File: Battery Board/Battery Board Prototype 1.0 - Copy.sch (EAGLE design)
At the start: 10 parts

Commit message: Added separation notches
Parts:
- added J1, J2: MPTC-02-16-02-6.30-XX-X-V, MPTC-02-16-02-6.30-XX-X-V:MPTC-02-16-02-6.30-XX-X-V
- added J3: TFM-107-01-XXX-D-DS, TFM-107-01-XXX-D-DS:TFM-107-01-XXX-D-DS
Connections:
- new net AUX0: U$1.PB1
- new net AUX1: U$1.PB2
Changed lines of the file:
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@@
 <part name="R6" library="resistor" library_urn="urn:adsk.eagle:library:348" deviceset="R-US_" device="R0805" package3d_urn="urn:adsk.eagle:package:23553/2"/>
 <part name="R7" library="resistor" library_urn="urn:adsk.eagle:library:348" deviceset="R-US_" device="R0805" package3d_urn="urn:adsk.eagle:package:23553/2"/>
+<part name="J1" library="MPTC-02-16-02-6.30-XX-X-V" deviceset="MPTC-02-16-02-6.30-XX-X-V" device=""/>
+<part name="J2" library="MPTC-02-16-02-6.30-XX-X-V" deviceset="MPTC-02-16-02-6.30-XX-X-V" device=""/>
+<part name="J3" library="TFM-107-01-XXX-D-DS" deviceset="TFM-107-01-XXX-D-DS" device=""/>
 </parts>
 <sheets>
@@
 <attribute name="VALUE" x="-52.07" y="-6.858" size="1.778" layer="96" rot="R180"/>
 </instance>
+<instance part="J1" gate="G$1" x="48.26" y="63.5" smashed="yes">
+<attribute name="NAME" x="38.1" y="80.01" size="1.778" layer="95"/>
+<attribute name="VALUE" x="38.1" y="43.18" size="1.778" layer="96"/>
+</instance>
+<instance part="J2" gate="G$1" x="127" y="50.8" smashed="yes">
+<attribute name="NAME" x="116.84" y="67.31" size="1.778" layer="95"/>
+<attribute name="VALUE" x="116.84" y="30.48" size="1.778" layer="96"/>
+</instance>
+<instance part="J3" gate="G$1" x="-50.8" y="78.74" smashed="yes">
+<attribute name="NAME" x="-45.72" y="82.042" size="1.27" layer="95"/>
+<attribute name="VALUE" x="-45.72" y="48.26" size="1.27" layer="96"/>
+</instance>
 </instances>
 <busses>
@@
 </segment>
 <segment>
-<wire x1="22.86" y1="35.56" x2="22.86" y2="27.94" width="0.1524" layer="91"/>
-<label x="22.86" y="27.94" size="1.27" layer="95" rot="R270" xref="yes"/>
+<wire x1="27.94" y1="35.56" x2="27.94" y2="27.94" width="0.1524" layer="91"/>
+<label x="27.94" y="27.94" size="1.27" layer="95" rot="R270" xref="yes"/>
 </segment>
 </net>
@@
 </segment>
 <segment>
-<wire x1="25.4" y1="27.94" x2="25.4" y2="35.56" width="0.1524" layer="91"/>
-<label x="25.4" y="27.94" size="1.27" layer="95" rot="R270" xref="yes"/>
+<wire x1="30.48" y1="27.94" x2="30.48" y2="35.56" width="0.1524" layer="91"/>
+<label x="30.48" y="27.94" size="1.27" layer="95" rot="R270" xref="yes"/>
 </segment>
 </net>
@@
 </segment>
 <segment>
-<wire x1="20.32" y1="35.56" x2="20.32" y2="27.94" width="0.1524" layer="91"/>
-<label x="20.32" y="27.94" size="1.27" layer="95" rot="R270" xref="yes"/>
+<wire x1="22.86" y1="35.56" x2="22.86" y2="27.94" width="0.1524" layer="91"/>
+<label x="22.86" y="27.94" size="1.27" layer="95" rot="R270" xref="yes"/>
 </segment>
 </net>
@@
 </segment>
 <segment>
-<wire x1="15.24" y1="27.94" x2="15.24" y2="35.56" width="0.1524" layer="91"/>
-<label x="15.24" y="27.94" size="1.27" layer="95" rot="R270" xref="yes"/>
+<wire x1="12.7" y1="27.94" x2="12.7" y2="35.56" width="0.1524" layer="91"/>
+<label x="12.7" y="27.94" size="1.27" layer="95" rot="R270" xref="yes"/>
 </segment>
 </net>
@@
 <label x="55.88" y="12.7" size="1.27" layer="95" rot="R270" xref="yes"/>
 </segment>
+<segment>
+<wire x1="15.24" y1="35.56" x2="15.24" y2="27.94" width="0.1524" layer="91"/>
+<label x="15.24" y="27.94" size="1.27" layer="95" rot="R270" xref="yes"/>
+</segment>
 </net>
 <net name="SDA" class="0">
@@
 </segment>
 </net>
+<net name="AUX1" class="0">
+<segment>
+<pinref part="U$1" gate="U$1" pin="PB2"/>
+<wire x1="20.32" y1="2.54" x2="22.86" y2="2.54" width="0.1524" layer="91"/>
+<label x="22.86" y="2.54" size="1.27" layer="95" xref="yes"/>
+</segment>
+<segment>
+<wire x1="20.32" y1="35.56" x2="20.32" y2="27.94" width="0.1524" layer="91"/>
+<label x="20.32" y="27.94" size="1.27" layer="95" rot="R270" xref="yes"/>
+</segment>
+</net>
+<net name="AUX0" class="0">
+<segment>
+<pinref part="U$1" gate="U$1" pin="PB1"/>
+<wire x1="20.32" y1="-2.54" x2="22.86" y2="-2.54" width="0.1524" layer="91"/>
+<label x="22.86" y="-2.54" size="1.27" layer="95" xref="yes"/>
+</segment>
+<segment>
+<wire x1="25.4" y1="35.56" x2="25.4" y2="27.94" width="0.1524" layer="91"/>
+<label x="25.4" y="27.94" size="1.27" layer="95" rot="R270" xref="yes"/>
+</segment>
+</net>

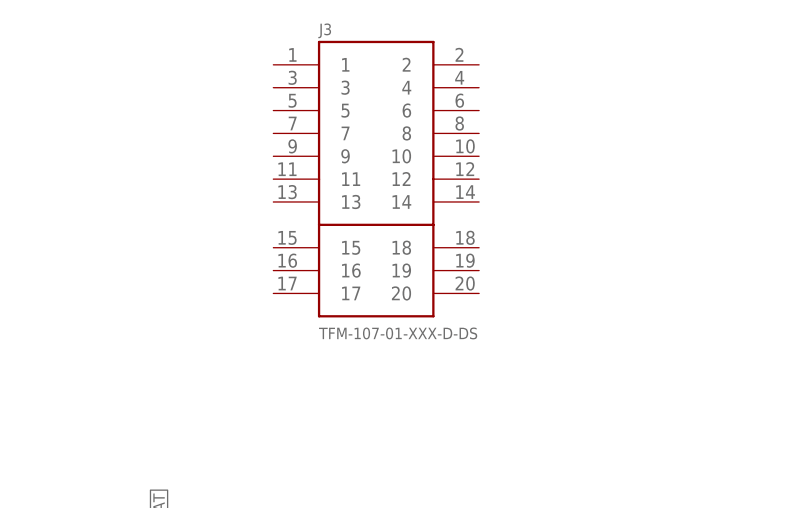
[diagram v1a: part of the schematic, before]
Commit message: Improved Battery board interface nets
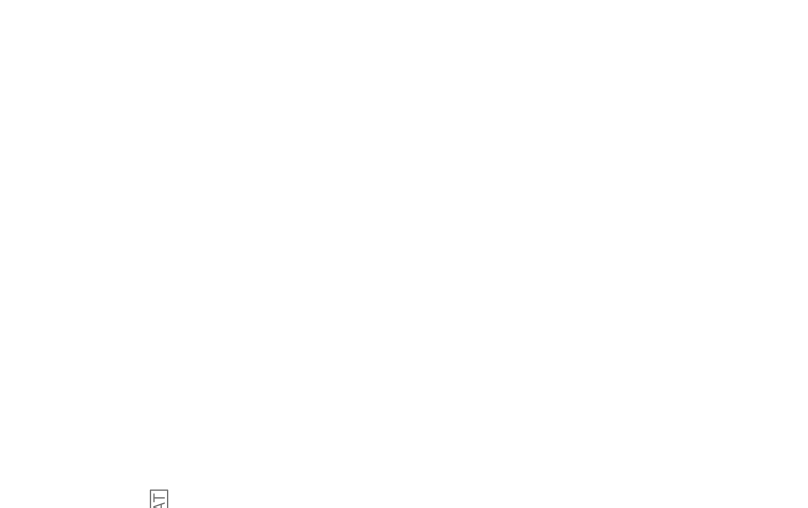
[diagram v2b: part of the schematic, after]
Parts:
- removed J3: TFM-107-01-XXX-D-DS, TFM-107-01-XXX-D-DS:TFM-107-01-XXX-D-DS
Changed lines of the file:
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@@
 <part name="J1" library="MPTC-02-16-02-6.30-XX-X-V" deviceset="MPTC-02-16-02-6.30-XX-X-V" device=""/>
 <part name="J2" library="MPTC-02-16-02-6.30-XX-X-V" deviceset="MPTC-02-16-02-6.30-XX-X-V" device=""/>
-<part name="J3" library="TFM-107-01-XXX-D-DS" deviceset="TFM-107-01-XXX-D-DS" device=""/>
 </parts>
 <sheets>
@@
 <attribute name="VALUE" x="116.84" y="30.48" size="1.778" layer="96"/>
 </instance>
-<instance part="J3" gate="G$1" x="-50.8" y="78.74" smashed="yes">
-<attribute name="NAME" x="-45.72" y="82.042" size="1.27" layer="95"/>
-<attribute name="VALUE" x="-45.72" y="48.26" size="1.27" layer="96"/>
-</instance>
 </instances>
